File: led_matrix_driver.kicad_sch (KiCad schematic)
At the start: 14 parts, among them J1 Conn_02x17_Odd_Even, J2 Screw_Terminal_01x02, J3 Screw_Terminal_01x02, J4 Conn_01x06_Pin, SW2 CK_KMS2xxGP, U2 Pico, U3 ESP32-WROOM-32, U4 74AHCT541, U5 74AHCT541, U6 Teensy4.0

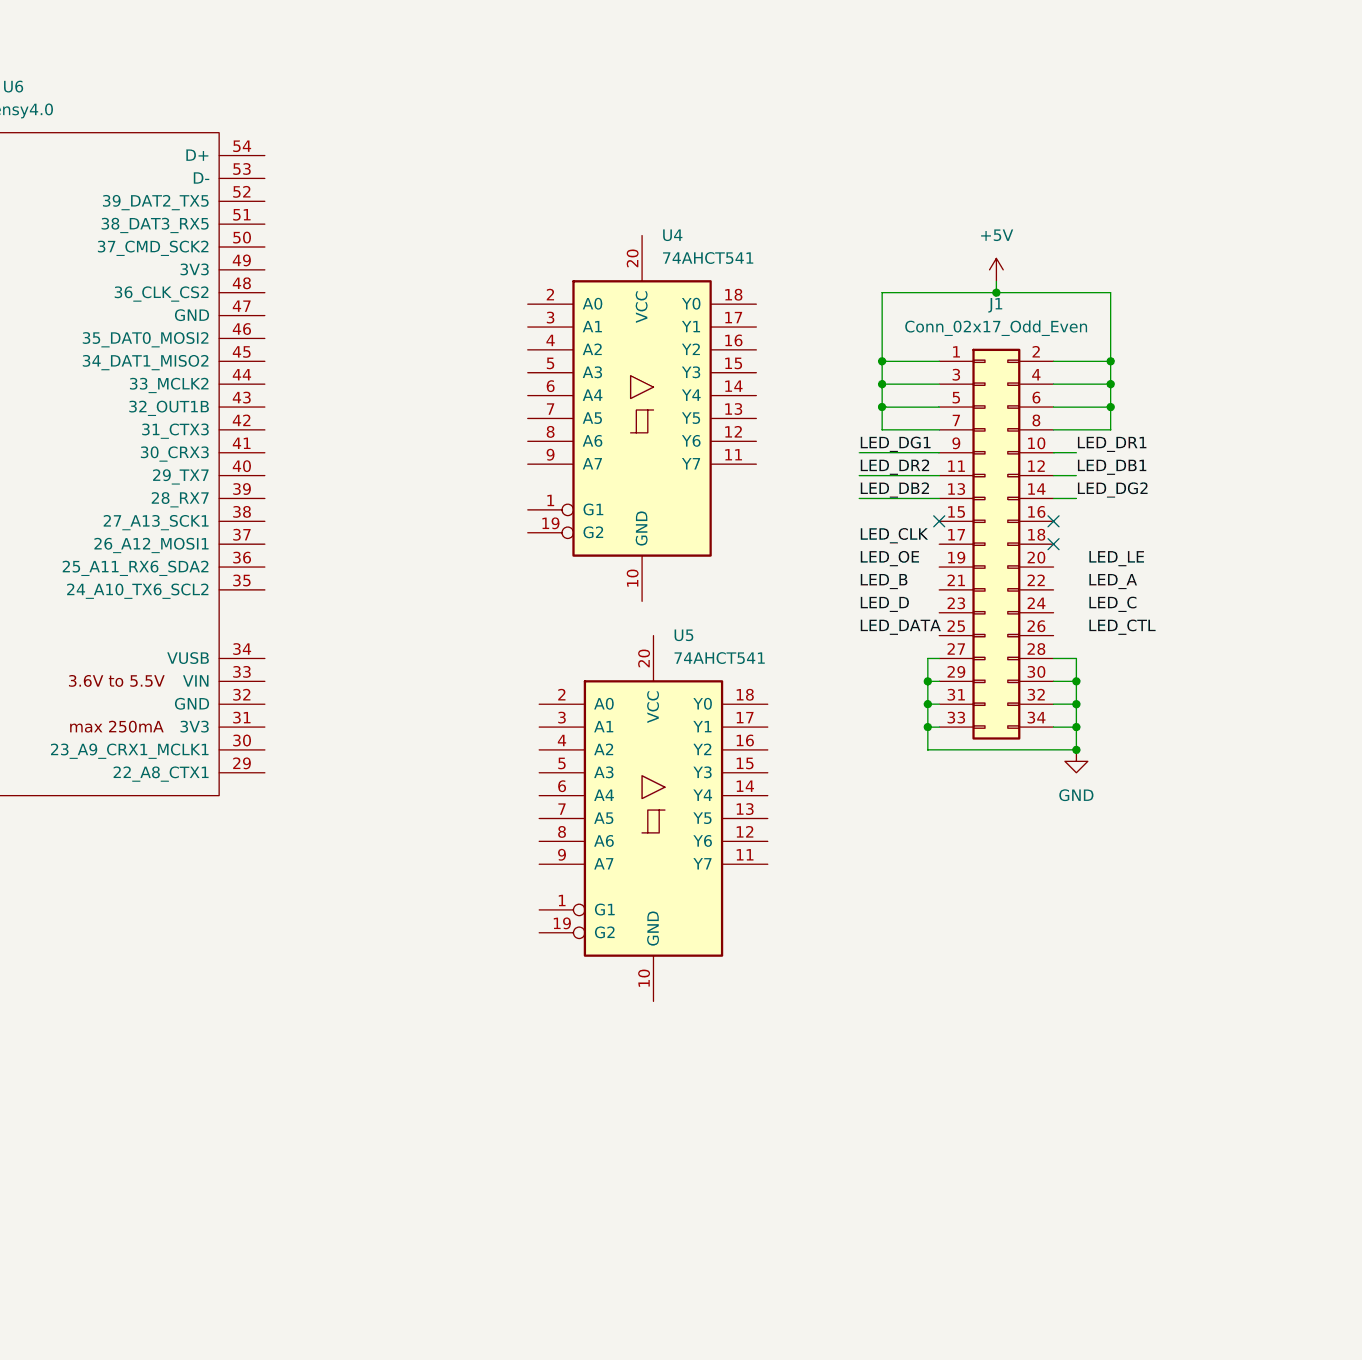
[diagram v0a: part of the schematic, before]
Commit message: Rearranged LED signals for easier layout
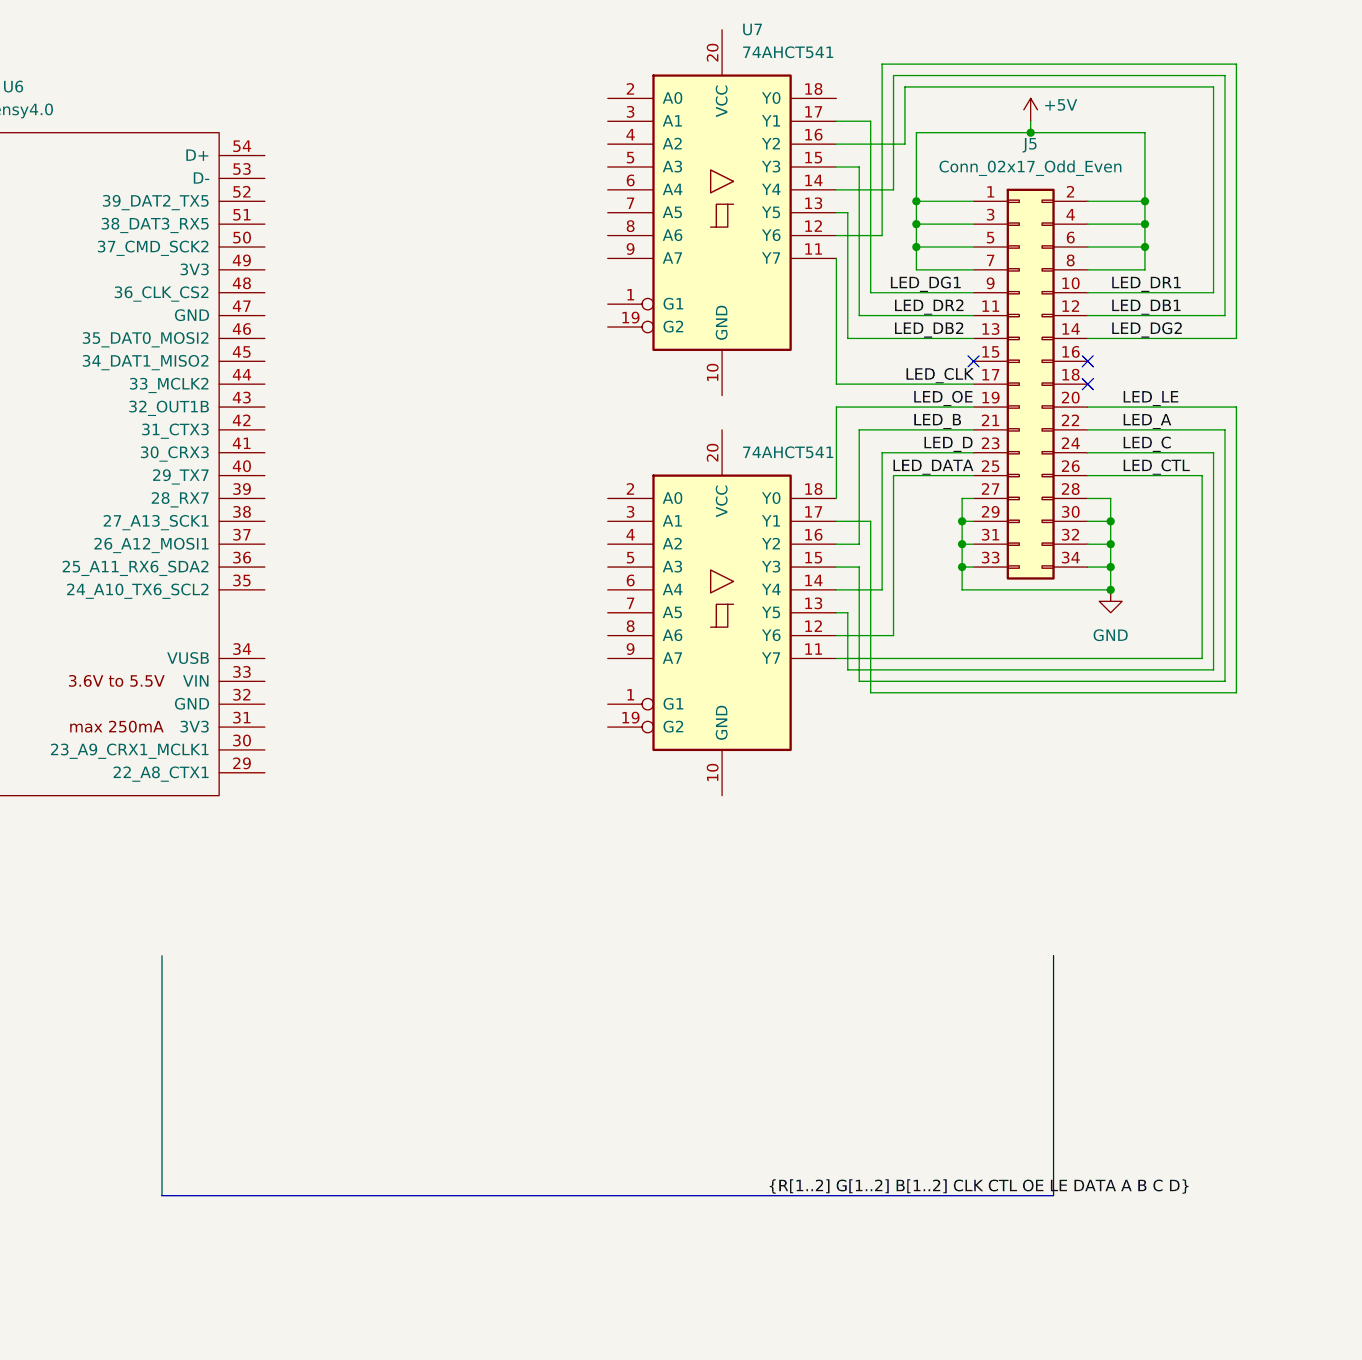
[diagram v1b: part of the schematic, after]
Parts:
- removed J1: Conn_02x17_Odd_Even, Connector_PinSocket_2.54mm:PinSocket_2x17_P2.54mm_Vertical, symbol Connector_Generic:Conn_02x17_Odd_Even
- removed U4, U5: 74AHCT541, Package_SO:SOIC-20W_7.5x12.8mm_P1.27mm, symbol 74xx:74AHCT541
- added J5: Conn_02x17_Odd_Even, Connector_PinSocket_2.54mm:PinSocket_2x17_P2.54mm_Vertical, symbol Connector_Generic:Conn_02x17_Odd_Even
- added U7, U8: 74AHCT541, Package_SO:SOIC-20W_7.5x12.8mm_P1.27mm, symbol 74xx:74AHCT541
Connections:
- net +5V: now also J5.1 (Pin_1), J5.2 (Pin_2), J5.3 (Pin_3), J5.4 (Pin_4), J5.5 (Pin_5), J5.6 (Pin_6), J5.7 (Pin_7), J5.8 (Pin_8)
- net GND: now also J5.27 (Pin_27), J5.28 (Pin_28), J5.29 (Pin_29), J5.30 (Pin_30), J5.31 (Pin_31), J5.32 (Pin_32), J5.33 (Pin_33), J5.34 (Pin_34)
- net LED_A: now also J5.22 (Pin_22), U8.15 (Y3)
- net LED_B: now also J5.21 (Pin_21), U8.16 (Y2)
- net LED_C: now also J5.24 (Pin_24), U8.13 (Y5)
- net LED_CLK: now also J5.17 (Pin_17), U7.11 (Y7)
- net LED_CTL: now also J5.26 (Pin_26), U8.11 (Y7)
- net LED_D: now also J5.23 (Pin_23), U8.14 (Y4)
- net LED_DATA: now also J5.25 (Pin_25), U8.12 (Y6)
- net LED_DB1: now also J5.12 (Pin_12), U7.14 (Y4)
- net LED_DB2: now also J5.13 (Pin_13), U7.13 (Y5)
- net LED_DG1: now also J5.9 (Pin_9), U7.17 (Y1)
- net LED_DG2: now also J5.14 (Pin_14), U7.12 (Y6)
- net LED_DR1: now also J5.10 (Pin_10), U7.16 (Y2)
- net LED_DR2: now also J5.11 (Pin_11), U7.15 (Y3)
- net LED_LE: now also J5.20 (Pin_20), U8.17 (Y1)
- net LED_OE: now also J5.19 (Pin_19), U8.18 (Y0)

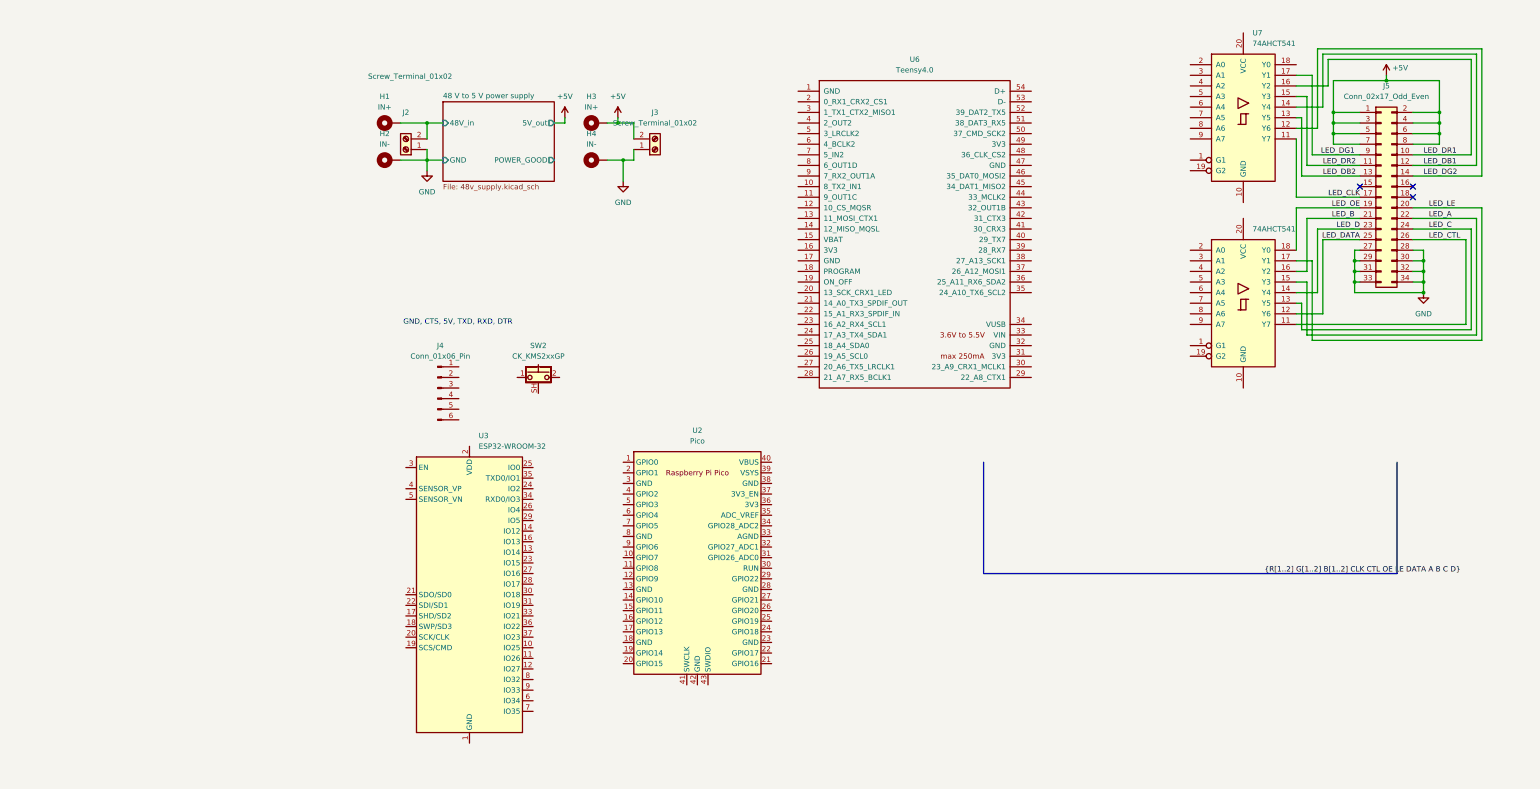
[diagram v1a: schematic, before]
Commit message: Added Teensy
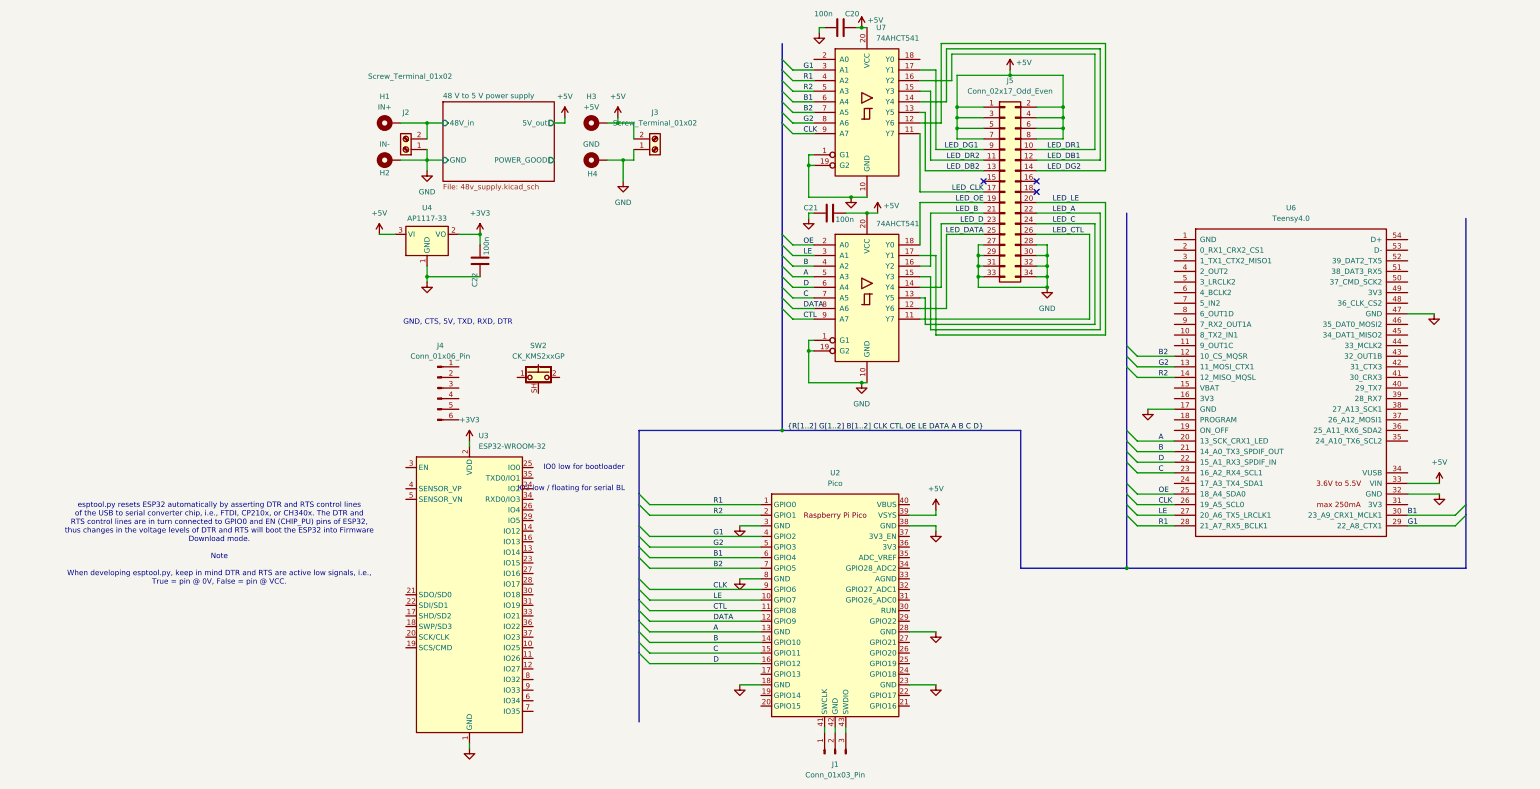
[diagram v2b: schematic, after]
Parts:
- added C20, C21, C22: 100n, Capacitor_SMD:C_0603_1608Metric, symbol Device:C
- added J1: Conn_01x03_Pin, Connector_PinHeader_2.54mm:PinHeader_1x03_P2.54mm_Vertical, symbol Connector:Conn_01x03_Pin
- added U4: AP1117-33, Package_TO_SOT_SMD:SOT-223-3_TabPin2, symbol Regulator_Linear:AP1117-50
- H1, H2: footprint (none) -> MountingHole:MountingHole_2.2mm_M2_DIN965_Pad
- H3: value IN+ -> +5V; footprint (none) -> MountingHole:MountingHole_2.2mm_M2_DIN965_Pad
- H4: value IN- -> GND; footprint (none) -> MountingHole:MountingHole_2.2mm_M2_DIN965_Pad
- J2, J3: footprint (none) -> Connector_Samtec_HPM_THT:Samtec_HPM-02-01-x-S_Straight_1x02_Pitch5.08mm
- J4: footprint (none) -> Connector_PinHeader_2.54mm:PinHeader_1x06_P2.54mm_Vertical
- U6: footprint (none) -> teensy:Teensy40_SMT
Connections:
- net +5V: now also U2.39 (VSYS), U6.33 (VIN), U7.20 (VCC), U8.20 (VCC), C20.2, C21.2, U4.3 (VI)
- net GND: now also U2.18 (GND), U2.23 (GND), U2.28 (GND), U2.3 (GND), U2.38 (GND), U2.8 (GND), U3.1 (GND), U3.15 (GND), U3.38 (GND), U3.39 (GND), U6.17 (GND), U6.32 (GND), U6.47 (GND), U7.1 (G1), U7.10 (GND), U7.19 (G2), U8.1 (G1), U8.10 (GND), U8.19 (G2), C20.1, C21.1, C22.1, U4.1 (GND)
- net OE: now reaches U8.2 (A0)
- net OE: now also U6.25 (18_A4_SDA0)
- net LE: now reaches U8.3 (A1)
- net LE: now also U2.10 (GPIO7), U6.27 (20_A6_TX5_LRCLK1)
- net B: now reaches U8.4 (A2)
- net B: now also U2.14 (GPIO10), U6.21 (14_A0_TX3_SPDIF_OUT)
- net A: now reaches U8.5 (A3)
- net A: now also U2.13 (GND), U6.20 (13_SCK_CRX1_LED)
- net D: now reaches U8.6 (A4)
- net D: now also U2.16 (GPIO12), U6.22 (15_A1_RX3_SPDIF_IN)
- net C: now reaches U8.7 (A5)
- net C: now also U2.15 (GPIO11), U6.23 (16_A2_RX4_SCL1)
- net DATA: now reaches U8.8 (A6)
- net DATA: now also U2.12 (GPIO9)
- net CTL: now reaches U8.9 (A7)
- net CTL: now also U2.11 (GPIO8)
- net R1: now reaches U2.1 (GPIO0)
- net R1: now also U6.28 (21_A7_RX5_BCLK1), U7.4 (A2)
- net R2: now reaches U2.2 (GPIO1)
- net R2: now also U6.14 (12_MISO_MQSL), U7.5 (A3)
- net G1: now reaches U2.4 (GPIO2)
- net G1: now also U6.29 (22_A8_CTX1), U7.3 (A1)
- net at U2.41 (SWCLK): now also J1.1 (Pin_1)
- net at U2.42 (GND): now also J1.2 (Pin_2)
- net at U2.43 (SWDIO): now also J1.3 (Pin_3)
- net G2: now reaches U2.5 (GPIO3)
- net G2: now also U6.13 (11_MOSI_CTX1), U7.8 (A6)
- net B1: now reaches U2.6 (GPIO4)
- net B1: now also U6.30 (23_A9_CRX1_MCLK1), U7.6 (A4)
- net B2: now reaches U2.7 (GPIO5)
- net B2: now also U6.12 (10_CS_MQSR), U7.7 (A5)
- net CLK: now reaches U2.9 (GPIO6)
- net CLK: now also U6.26 (19_A5_SCL0), U7.9 (A7)
- net +3V3: now reaches U3.2 (VDD)
- net +3V3: now also C22.2, U4.2 (VO)
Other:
- note added: "IO0 low for bootloader"
- note added: "IO2 low / floating for serial BL"
- note added: "esptool.py resets ESP32 automatically by asserting DTR and RTS control lines of the USB to serial converter chip, i.e., FTDI, CP210x, or CH340x. The DTR and RTS control lines are in turn connected to GPIO0 and EN (CHIP_PU) pins of ESP32, thus changes in the voltage levels of DTR and RTS will boot the ESP32 into Firmware Download mode. Note When developing esptool.py, keep in mind DTR and RTS are 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"
- moved on the sheet: J5, U2, U6, U7

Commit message: Routed data signals. Remove calibration data I2C wires
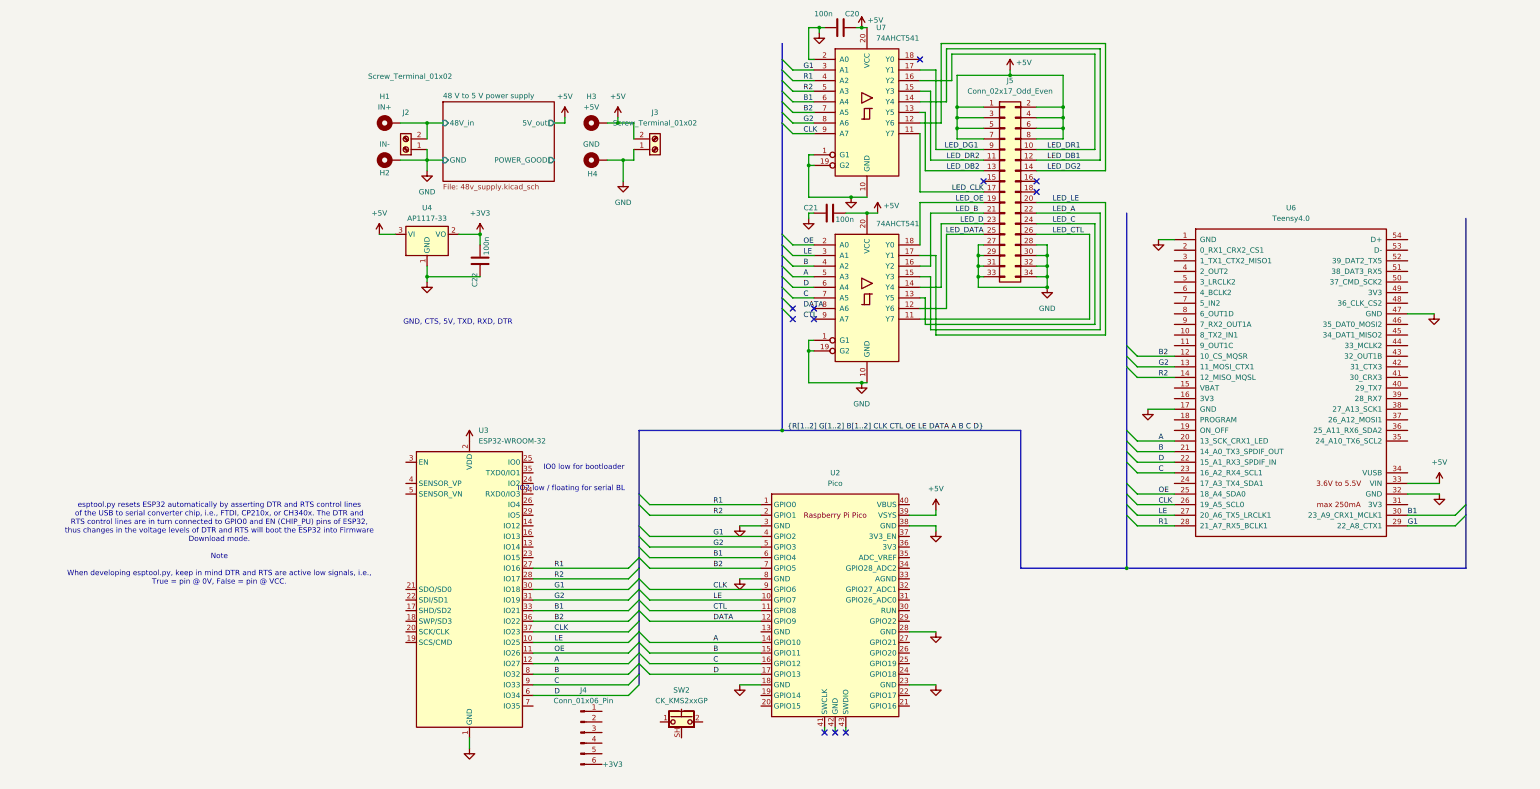
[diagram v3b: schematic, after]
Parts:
- removed J1: Conn_01x03_Pin, Connector_PinHeader_2.54mm:PinHeader_1x03_P2.54mm_Vertical, symbol Connector:Conn_01x03_Pin
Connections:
- net A: now also U2.14 (GPIO10), U3.12 (IO27); no longer U2.13 (GND)
- net B: now also U2.15 (GPIO11), U3.8 (IO32); no longer U2.14 (GPIO10)
- net B1: now also U3.33 (IO21)
- net B2: now also U3.36 (IO22)
- net C: now also U2.16 (GPIO12), U3.9 (IO33); no longer U2.15 (GPIO11)
- net CLK: now also U3.37 (IO23)
- net CTL: no longer U8.9 (A7)
- net D: now also U2.17 (GPIO13), U3.6 (IO34); no longer U2.16 (GPIO12)
- net DATA: no longer U8.8 (A6)
- net G1: now also U3.30 (IO18)
- net G2: now also U3.31 (IO19)
- net GND: now also U6.1 (GND), U7.2 (A0)
- net LE: now also U3.10 (IO25)
- net OE: now also U3.11 (IO26)
- net R1: now also U3.27 (IO16)
- net R2: now also U3.28 (IO17)
- no-connect marks 3 -> 11
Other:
- moved on the sheet: J4, SW2, U3
